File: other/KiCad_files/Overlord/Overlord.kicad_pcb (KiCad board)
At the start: 2 copper layers, 155.1 x 86.1 mm, 108 parts, among them J1 RJ45x2, J2 Screw_Terminal_01x09, J3 Conn_01x12_Female, J4 Screw_Terminal_01x09, J5 Screw_Terminal_01x09, J6 Screw_Terminal_01x09, J7 USB_B, J8 USB_cable, Q1 2N7002E, Q2 2N7002E, Q3 2N7002E, Q4 2N7002E, U1 74HC4052D,653, U2 74HC4052D,653, U3 74HC4052D,653, U4 74HC4052D,653, U5 LM2575D2T-5G, U6 SN65HVD230, U7 MAX485ESA+T, U8 AP63203WU-7, U9 MAX485ESA+T

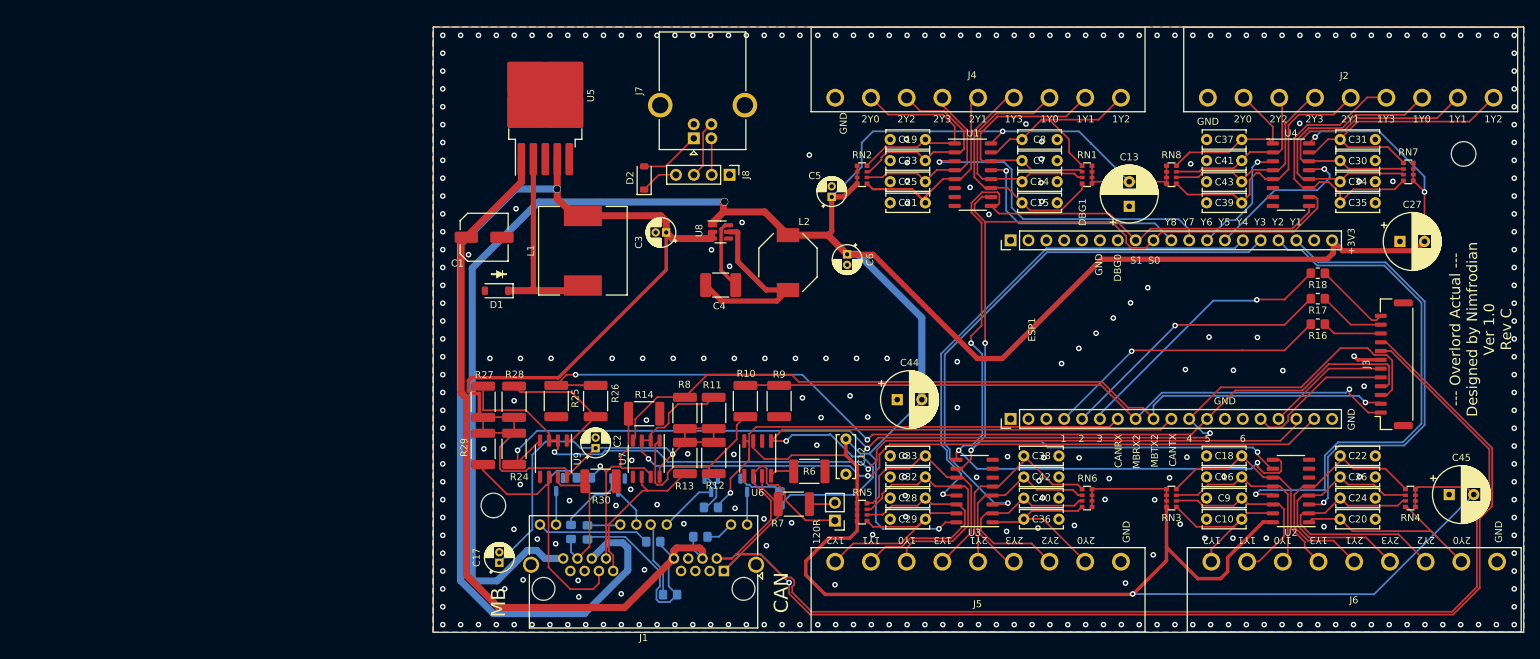
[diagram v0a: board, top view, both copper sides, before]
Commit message: sent to production
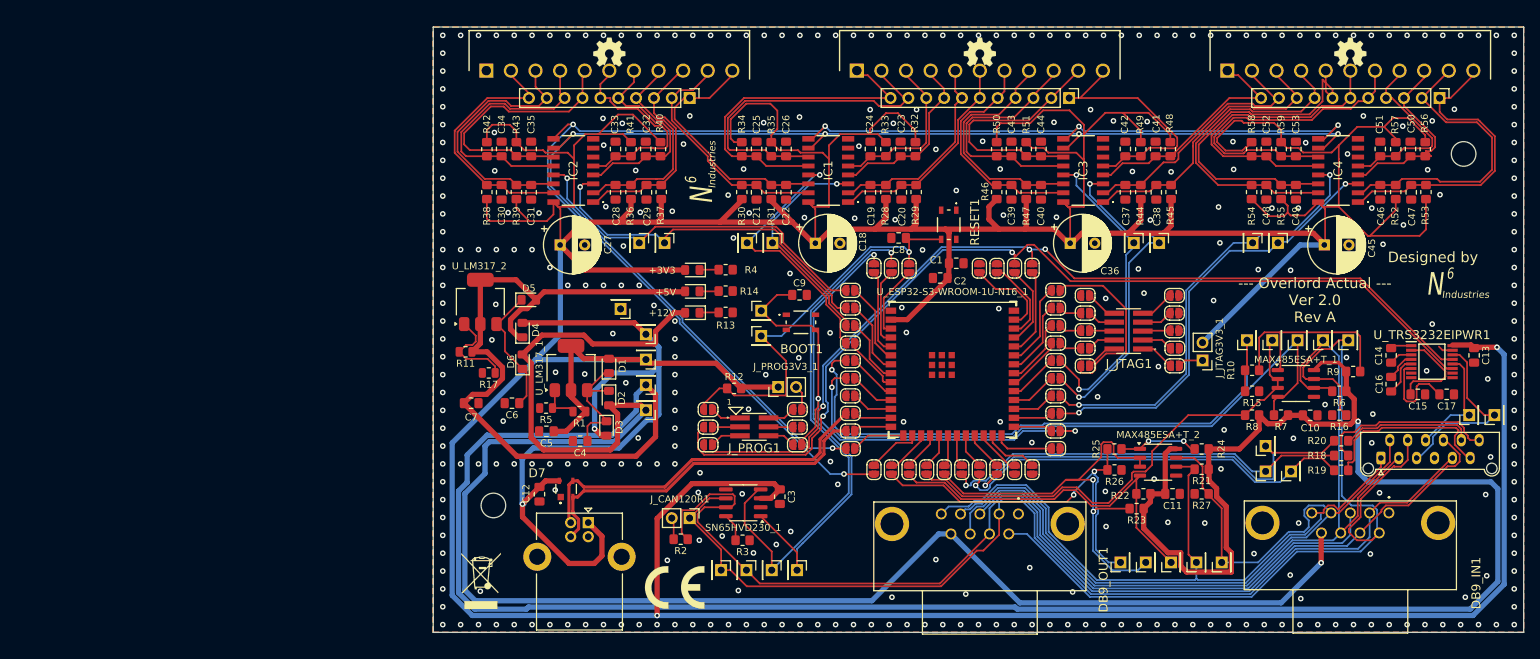
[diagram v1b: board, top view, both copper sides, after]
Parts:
- removed 120R_enable1: Conn_01x02_Male, Connector_PinHeader_2.54mm:PinHeader_1x02_P2.54mm_Vertical
- removed ESP1: ESP-DevKitC-V4, Overlord:ESP32-DevKitC-V4
- removed J8: USB_cable, Connector_PinHeader_2.54mm:PinHeader_1x04_P2.54mm_Vertical
- removed L1: 7447709331, Inductor_SMD:L_12x12mm_H8mm
- removed L2: 4.7uH, Inductor_SMD:L_Bourns-SRU8028_8.0x8.0mm
- removed Q1, Q2, Q3, Q4: 2N7002E, Package_TO_SOT_SMD:SOT-23
- removed RN1, RN2, RN3, RN4, RN5, RN6, RN7, RN8: Res_network 4.7kOhm, Resistor_SMD:R_Array_Convex_4x0612
- removed U1, U2, U3, U4: 74HC4052D,653, Package_SO:SO-16_3.9x9.9mm_P1.27mm
- removed U5: LM2575D2T-5G, Package_TO_SOT_SMD:TO-263-5_TabPin3
- removed U6: SN65HVD230, Package_SO:SOIC-8_3.9x4.9mm_P1.27mm
- removed U7, U9: MAX485ESA+T, Package_SO:SO-8_3.9x4.9mm_P1.27mm
- removed U8: AP63203WU-7, Package_TO_SOT_SMD:TSOT-23-6
- added 12VLED1: LED, LED_SMD:LED_0805_2012Metric_Pad1.15x1.40mm_HandSolder, F.Cu at (62.2, 66.0)
- added 3V3LED1: LED, LED_SMD:LED_0805_2012Metric_Pad1.15x1.40mm_HandSolder, F.Cu at (62.2, 60.0)
- added 5VLED1: LED, LED_SMD:LED_0805_2012Metric_Pad1.15x1.40mm_HandSolder, F.Cu at (62.2, 63.0)
- added BOOT1: PTS810SJK250SMTR LFS, OverlordCommon:PTS810SJK250SMTRLFS, F.Cu at (77.7, 67.4)
- added C11: 10uF, Capacitor_SMD:C_0805_2012Metric_Pad1.18x1.45mm_HandSolder, F.Cu at (130.6, 91.8)
- added C46: 0.1uF, Capacitor_SMD:C_0805_2012Metric_Pad1.18x1.45mm_HandSolder, F.Cu at (160.1, 48.9)
- added C47: 0.1uF, Capacitor_SMD:C_0805_2012Metric_Pad1.18x1.45mm_HandSolder, F.Cu at (164.5, 48.9)
- added C48: 0.1uF, Capacitor_SMD:C_0805_2012Metric_Pad1.18x1.45mm_HandSolder, F.Cu at (143.9, 48.9)
- added C49: 0.1uF, Capacitor_SMD:C_0805_2012Metric_Pad1.18x1.45mm_HandSolder, F.Cu at (148.1, 48.9)
- added C50: 0.1uF, Capacitor_SMD:C_0805_2012Metric_Pad1.18x1.45mm_HandSolder, F.Cu at (164.4, 42.7)
- added C51: 0.1uF, Capacitor_SMD:C_0805_2012Metric_Pad1.18x1.45mm_HandSolder, F.Cu at (160.1, 42.7)
- added C52: 0.1uF, Capacitor_SMD:C_0805_2012Metric_Pad1.18x1.45mm_HandSolder, F.Cu at (143.9, 42.7)
- added C53: 0.1uF, Capacitor_SMD:C_0805_2012Metric_Pad1.18x1.45mm_HandSolder, F.Cu at (148.1, 42.7)
- added D3: 1N4148, Diode_SMD:D_0805_2012Metric_Pad1.15x1.40mm_HandSolder, F.Cu at (50.0, 82.5)
- added D4: 1N4148, Diode_SMD:D_0805_2012Metric_Pad1.15x1.40mm_HandSolder, F.Cu at (38.1, 68.5)
- added D5: 1N4148, Diode_SMD:D_0805_2012Metric_Pad1.15x1.40mm_HandSolder, F.Cu at (39.0, 64.2)
- added D6: 1N4148, Diode_SMD:D_0805_2012Metric_Pad1.15x1.40mm_HandSolder, F.Cu at (38.1, 73.0)
- added D7: TPD2E001DZDR, OverlordCommon:TPD2E001DZDR, F.Cu at (44.3, 91.1)
- added DB9_IN1: 5788792-2, OverlordCommon:5788792, F.Cu at (155.8, 101.9)
- added DB9_OUT1: 5747844-4, OverlordCommon:57478444, F.Cu at (103.2, 102.0)
- added Dbg1: Connector_Conn_01x01_Male, Connector_PinHeader_2.54mm:PinHeader_1x01_P2.54mm_Vertical, F.Cu at (125.1, 56.1)
- added Dbg10: Connector_Conn_01x01_Male, Connector_PinHeader_2.54mm:PinHeader_1x01_P2.54mm_Vertical, F.Cu at (155.6, 70.0)
- added Dbg11: Connector_Conn_01x01_Male, Connector_PinHeader_2.54mm:PinHeader_1x01_P2.54mm_Vertical, F.Cu at (58.3, 56.1)
- added Dbg12: Connector_Conn_01x01_Male, Connector_PinHeader_2.54mm:PinHeader_1x01_P2.54mm_Vertical, F.Cu at (123.2, 101.5)
- added Dbg13: Connector_Conn_01x01_Male, Connector_PinHeader_2.54mm:PinHeader_1x01_P2.54mm_Vertical, F.Cu at (141.9, 56.1)
- added Dbg14: Connector_Conn_01x01_Male, Connector_PinHeader_2.54mm:PinHeader_1x01_P2.54mm_Vertical, F.Cu at (126.8, 101.5)
- added Dbg15: Connector_Conn_01x01_Male, Connector_PinHeader_2.54mm:PinHeader_1x01_P2.54mm_Vertical, F.Cu at (145.6, 56.1)
- added Dbg16: Connector_Conn_01x01_Male, Connector_PinHeader_2.54mm:PinHeader_1x01_P2.54mm_Vertical, F.Cu at (130.3, 101.5)
- added Dbg17: Connector_Conn_01x01_Male, Connector_PinHeader_2.54mm:PinHeader_1x01_P2.54mm_Vertical, F.Cu at (133.9, 101.5)
- added Dbg18: Connector_Conn_01x01_Male, Connector_PinHeader_2.54mm:PinHeader_1x01_P2.54mm_Vertical, F.Cu at (137.6, 101.5)
- added Dbg19: Connector_Conn_01x01_Male, Connector_PinHeader_2.54mm:PinHeader_1x01_P2.54mm_Vertical, F.Cu at (52.0, 65.5)
- added Dbg2: Connector_Conn_01x01_Male, Connector_PinHeader_2.54mm:PinHeader_1x01_P2.54mm_Vertical, F.Cu at (141.2, 70.0)
- added Dbg20: Connector_Conn_01x01_Male, Connector_PinHeader_2.54mm:PinHeader_1x01_P2.54mm_Vertical, F.Cu at (77.1, 102.7)
- added Dbg21: Connector_Conn_01x01_Male, Connector_PinHeader_2.54mm:PinHeader_1x01_P2.54mm_Vertical, F.Cu at (73.5, 102.7)
- added Dbg22: Connector_Conn_01x01_Male, Connector_PinHeader_2.54mm:PinHeader_1x01_P2.54mm_Vertical, F.Cu at (70.0, 102.7)
- added Dbg23: Connector_Conn_01x01_Male, Connector_PinHeader_2.54mm:PinHeader_1x01_P2.54mm_Vertical, F.Cu at (55.6, 69.1)
- added Dbg24: Connector_Conn_01x01_Male, Connector_PinHeader_2.54mm:PinHeader_1x01_P2.54mm_Vertical, F.Cu at (66.3, 102.7)
- added Dbg25: Connector_Conn_01x01_Male, Connector_PinHeader_2.54mm:PinHeader_1x01_P2.54mm_Vertical, F.Cu at (72.0, 69.3)
- added Dbg26: Connector_Conn_01x01_Male, Connector_PinHeader_2.54mm:PinHeader_1x01_P2.54mm_Vertical, F.Cu at (72.0, 65.8)
- added Dbg27: Connector_Conn_01x01_Male, Connector_PinHeader_2.54mm:PinHeader_1x01_P2.54mm_Vertical, F.Cu at (55.6, 72.7)
- added Dbg28: Connector_Conn_01x01_Male, Connector_PinHeader_2.54mm:PinHeader_1x01_P2.54mm_Vertical, F.Cu at (143.8, 88.6)
- added Dbg29: Connector_Conn_01x01_Male, Connector_PinHeader_2.54mm:PinHeader_1x01_P2.54mm_Vertical, F.Cu at (147.4, 88.6)
- added Dbg3: Connector_Conn_01x01_Male, Connector_PinHeader_2.54mm:PinHeader_1x01_P2.54mm_Vertical, F.Cu at (128.7, 56.1)
- added Dbg30: Connector_Conn_01x01_Male, Connector_PinHeader_2.54mm:PinHeader_1x01_P2.54mm_Vertical, F.Cu at (55.6, 76.3)
- added Dbg31: Connector_Conn_01x01_Male, Connector_PinHeader_2.54mm:PinHeader_1x01_P2.54mm_Vertical, F.Cu at (143.8, 85.0)
- added Dbg32: Connector_Conn_01x01_Male, Connector_PinHeader_2.54mm:PinHeader_1x01_P2.54mm_Vertical, F.Cu at (172.7, 80.6)
- added Dbg33: Connector_Conn_01x01_Male, Connector_PinHeader_2.54mm:PinHeader_1x01_P2.54mm_Vertical, F.Cu at (55.6, 79.9)
- added Dbg34: Connector_Conn_01x01_Male, Connector_PinHeader_2.54mm:PinHeader_1x01_P2.54mm_Vertical, F.Cu at (176.3, 80.6)
- added Dbg4: Connector_Conn_01x01_Male, Connector_PinHeader_2.54mm:PinHeader_1x01_P2.54mm_Vertical, F.Cu at (144.8, 70.0)
- added Dbg5: Connector_Conn_01x01_Male, Connector_PinHeader_2.54mm:PinHeader_1x01_P2.54mm_Vertical, F.Cu at (70.0, 56.1)
- added Dbg6: Connector_Conn_01x01_Male, Connector_PinHeader_2.54mm:PinHeader_1x01_P2.54mm_Vertical, F.Cu at (148.3, 70.0)
- added Dbg7: Connector_Conn_01x01_Male, Connector_PinHeader_2.54mm:PinHeader_1x01_P2.54mm_Vertical, F.Cu at (73.7, 56.1)
- added Dbg8: Connector_Conn_01x01_Male, Connector_PinHeader_2.54mm:PinHeader_1x01_P2.54mm_Vertical, F.Cu at (151.9, 70.0)
- added Dbg9: Connector_Conn_01x01_Male, Connector_PinHeader_2.54mm:PinHeader_1x01_P2.54mm_Vertical, F.Cu at (54.7, 56.1)
- added IC1: 74HC4052D,653, OverlordCommon:74HC4052D653, F.Cu at (81.6, 45.8)
- added IC2: 74HC4052D,653, OverlordCommon:74HC4052D653, F.Cu at (45.3, 45.8)
- added IC3: 74HC4052D,653, OverlordCommon:74HC4052D653, F.Cu at (117.8, 45.8)
- added IC4: 74HC4052D,653, OverlordCommon:74HC4052D653, F.Cu at (154.1, 45.8)
- added JP1: SolderJumper_2_Open, Jumper:SolderJumper-2_P1.3mm_Open_RoundedPad1.0x1.5mm, F.Cu at (103.1, 59.7)
- added JP10: SolderJumper_2_Open, Jumper:SolderJumper-2_P1.3mm_Open_RoundedPad1.0x1.5mm, F.Cu at (84.7, 65.4)
- added JP11: SolderJumper_2_Open, Jumper:SolderJumper-2_P1.3mm_Open_RoundedPad1.0x1.5mm, F.Cu at (113.9, 65.4)
- added JP12: SolderJumper_2_Open, Jumper:SolderJumper-2_P1.3mm_Open_RoundedPad1.0x1.5mm, F.Cu at (84.7, 67.9)
- added JP13: SolderJumper_2_Open, Jumper:SolderJumper-2_P1.3mm_Open_RoundedPad1.0x1.5mm, F.Cu at (113.9, 67.9)
- added JP14: SolderJumper_2_Open, Jumper:SolderJumper-2_P1.3mm_Open_RoundedPad1.0x1.5mm, F.Cu at (84.7, 70.4)
- added JP15: SolderJumper_2_Open, Jumper:SolderJumper-2_P1.3mm_Open_RoundedPad1.0x1.5mm, F.Cu at (113.9, 70.4)
- added JP16: SolderJumper_2_Open, Jumper:SolderJumper-2_P1.3mm_Open_RoundedPad1.0x1.5mm, F.Cu at (84.7, 72.9)
- added JP17: SolderJumper_2_Open, Jumper:SolderJumper-2_P1.3mm_Open_RoundedPad1.0x1.5mm, F.Cu at (113.9, 72.9)
- added JP18: SolderJumper_2_Open, Jumper:SolderJumper-2_P1.3mm_Open_RoundedPad1.0x1.5mm, F.Cu at (84.7, 75.4)
- added JP19: SolderJumper_2_Open, Jumper:SolderJumper-2_P1.3mm_Open_RoundedPad1.0x1.5mm, F.Cu at (113.9, 75.4)
- added JP2: SolderJumper_2_Open, Jumper:SolderJumper-2_P1.3mm_Open_RoundedPad1.0x1.5mm, F.Cu at (93.1, 59.7)
- added JP20: SolderJumper_2_Open, Jumper:SolderJumper-2_P1.3mm_Open_RoundedPad1.0x1.5mm, F.Cu at (84.7, 77.9)
- added JP21: SolderJumper_2_Open, Jumper:SolderJumper-2_P1.3mm_Open_RoundedPad1.0x1.5mm, F.Cu at (113.9, 77.9)
- added JP22: SolderJumper_2_Open, Jumper:SolderJumper-2_P1.3mm_Open_RoundedPad1.0x1.5mm, F.Cu at (84.7, 80.4)
- added JP23: SolderJumper_2_Open, Jumper:SolderJumper-2_P1.3mm_Open_RoundedPad1.0x1.5mm, F.Cu at (113.9, 80.4)
- added JP24: SolderJumper_2_Open, Jumper:SolderJumper-2_P1.3mm_Open_RoundedPad1.0x1.5mm, F.Cu at (84.7, 82.9)
- added JP25: SolderJumper_2_Open, Jumper:SolderJumper-2_P1.3mm_Open_RoundedPad1.0x1.5mm, F.Cu at (113.9, 82.9)
- added JP26: SolderJumper_2_Open, Jumper:SolderJumper-2_P1.3mm_Open_RoundedPad1.0x1.5mm, F.Cu at (84.7, 85.4)
- added JP27: SolderJumper_2_Open, Jumper:SolderJumper-2_P1.3mm_Open_RoundedPad1.0x1.5mm, F.Cu at (88.1, 88.4)
- added JP28: SolderJumper_2_Open, Jumper:SolderJumper-2_P1.3mm_Open_RoundedPad1.0x1.5mm, F.Cu at (90.6, 88.4)
- added JP29: SolderJumper_2_Open, Jumper:SolderJumper-2_P1.3mm_Open_RoundedPad1.0x1.5mm, F.Cu at (93.1, 88.4)
- added JP3: SolderJumper_2_Open, Jumper:SolderJumper-2_P1.3mm_Open_RoundedPad1.0x1.5mm, F.Cu at (105.6, 59.7)
- added JP30: SolderJumper_2_Open, Jumper:SolderJumper-2_P1.3mm_Open_RoundedPad1.0x1.5mm, F.Cu at (95.6, 88.4)
- added JP31: SolderJumper_2_Open, Jumper:SolderJumper-2_P1.3mm_Open_RoundedPad1.0x1.5mm, F.Cu at (98.1, 88.4)
- added JP32: SolderJumper_2_Open, Jumper:SolderJumper-2_P1.3mm_Open_RoundedPad1.0x1.5mm, F.Cu at (100.6, 88.4)
- added JP33: SolderJumper_2_Open, Jumper:SolderJumper-2_P1.3mm_Open_RoundedPad1.0x1.5mm, F.Cu at (103.1, 88.4)
- added JP34: SolderJumper_2_Open, Jumper:SolderJumper-2_P1.3mm_Open_RoundedPad1.0x1.5mm, F.Cu at (105.6, 88.4)
- added JP35: SolderJumper_2_Open, Jumper:SolderJumper-2_P1.3mm_Open_RoundedPad1.0x1.5mm, F.Cu at (108.1, 88.4)
- added JP36: SolderJumper_2_Open, Jumper:SolderJumper-2_P1.3mm_Open_RoundedPad1.0x1.5mm, F.Cu at (110.6, 88.4)
- added JP37: SolderJumper_2_Open, Jumper:SolderJumper-2_P1.3mm_Open_RoundedPad1.0x1.5mm, F.Cu at (113.9, 85.4)
- added JP38: SolderJumper_2_Open, Jumper:SolderJumper-2_P1.3mm_Open_RoundedPad1.0x1.5mm, F.Cu at (130.9, 73.6)
- added JP39: SolderJumper_2_Open, Jumper:SolderJumper-2_P1.3mm_Open_RoundedPad1.0x1.5mm, F.Cu at (118.1, 73.6)
- added JP4: SolderJumper_2_Open, Jumper:SolderJumper-2_P1.3mm_Open_RoundedPad1.0x1.5mm, F.Cu at (90.6, 59.7)
- added JP40: SolderJumper_2_Open, Jumper:SolderJumper-2_P1.3mm_Open_RoundedPad1.0x1.5mm, F.Cu at (130.9, 71.1)
- added JP41: SolderJumper_2_Open, Jumper:SolderJumper-2_P1.3mm_Open_RoundedPad1.0x1.5mm, F.Cu at (118.1, 71.1)
- added JP42: SolderJumper_2_Open, Jumper:SolderJumper-2_P1.3mm_Open_RoundedPad1.0x1.5mm, F.Cu at (130.8, 68.6)
- added JP43: SolderJumper_2_Open, Jumper:SolderJumper-2_P1.3mm_Open_RoundedPad1.0x1.5mm, F.Cu at (118.1, 68.6)
- added JP44: SolderJumper_2_Open, Jumper:SolderJumper-2_P1.3mm_Open_RoundedPad1.0x1.5mm, F.Cu at (130.8, 66.1)
- added JP45: SolderJumper_2_Open, Jumper:SolderJumper-2_P1.3mm_Open_RoundedPad1.0x1.5mm, F.Cu at (118.1, 66.1)
- added JP46: SolderJumper_2_Open, Jumper:SolderJumper-2_P1.3mm_Open_RoundedPad1.0x1.5mm, F.Cu at (130.8, 63.6)
- added JP47: SolderJumper_2_Open, Jumper:SolderJumper-2_P1.3mm_Open_RoundedPad1.0x1.5mm, F.Cu at (118.1, 63.6)
- added JP48: SolderJumper_2_Open, Jumper:SolderJumper-2_P1.3mm_Open_RoundedPad1.0x1.5mm, F.Cu at (64.5, 79.8)
- added JP49: SolderJumper_2_Open, Jumper:SolderJumper-2_P1.3mm_Open_RoundedPad1.0x1.5mm, F.Cu at (77.2, 79.8)
- added JP5: SolderJumper_2_Open, Jumper:SolderJumper-2_P1.3mm_Open_RoundedPad1.0x1.5mm, F.Cu at (108.1, 59.7)
- added JP50: SolderJumper_2_Open, Jumper:SolderJumper-2_P1.3mm_Open_RoundedPad1.0x1.5mm, F.Cu at (64.5, 82.3)
- added JP51: SolderJumper_2_Open, Jumper:SolderJumper-2_P1.3mm_Open_RoundedPad1.0x1.5mm, F.Cu at (77.2, 82.3)
- added JP52: SolderJumper_2_Open, Jumper:SolderJumper-2_P1.3mm_Open_RoundedPad1.0x1.5mm, F.Cu at (64.5, 84.8)
- added JP53: SolderJumper_2_Open, Jumper:SolderJumper-2_P1.3mm_Open_RoundedPad1.0x1.5mm, F.Cu at (77.2, 84.8)
- added JP6: SolderJumper_2_Open, Jumper:SolderJumper-2_P1.3mm_Open_RoundedPad1.0x1.5mm, F.Cu at (88.1, 59.7)
- added JP7: SolderJumper_2_Open, Jumper:SolderJumper-2_P1.3mm_Open_RoundedPad1.0x1.5mm, F.Cu at (110.6, 59.7)
- added JP8: SolderJumper_2_Open, Jumper:SolderJumper-2_P1.3mm_Open_RoundedPad1.0x1.5mm, F.Cu at (84.7, 62.9)
- added JP9: SolderJumper_2_Open, Jumper:SolderJumper-2_P1.3mm_Open_RoundedPad1.0x1.5mm, F.Cu at (113.9, 62.9)
- added J_CAN120R1: Conn_01x02_Male, Connector_PinHeader_2.54mm:PinHeader_1x02_P2.54mm_Vertical, F.Cu at (61.9, 95.2)
- added J_JTAG1: FTSH-105-01-S-DV-K, OverlordCommon:FTSH-105-XX-YYY-DV-K, F.Cu at (124.3, 68.7)
- added J_JTAG3V3_1: Conn_01x02_Pin, Connector_PinHeader_2.54mm:PinHeader_1x02_P2.54mm_Vertical, F.Cu at (134.8, 72.8)
- added J_PROG1: FTSH-103-01-S-DV-TR, OverlordCommon:FTSH-103-XX-YYY-DV-TR, F.Cu at (71.1, 82.3)
- added J_PROG3V3_1: Conn_01x02_Pin, Connector_PinHeader_2.54mm:PinHeader_1x02_P2.54mm_Vertical, F.Cu at (74.5, 76.6)
- added J_USB1: USB_B, OverlordCommon:USB, F.Cu at (46.2, 102.9)
- added MAX485ESA+T_1: MAX485ESA+T, Package_SO:SO-8_3.9x4.9mm_P1.27mm, F.Cu at (148.1, 76.1)
- added MAX485ESA+T_2: MAX485ESA+T, Package_SO:SO-8_3.9x4.9mm_P1.27mm, F.Cu at (128.5, 87.3)
- added R19: 220, Resistor_SMD:R_0805_2012Metric_Pad1.20x1.40mm_HandSolder, F.Cu at (154.6, 88.5)
- added R20: 220, Resistor_SMD:R_0805_2012Metric_Pad1.20x1.40mm_HandSolder, F.Cu at (154.6, 84.2)
- added R21: 20K, Resistor_SMD:R_0805_2012Metric_Pad1.20x1.40mm_HandSolder, F.Cu at (134.7, 88.3)
- added R22: 10K, Resistor_SMD:R_0805_2012Metric_Pad1.20x1.40mm_HandSolder, F.Cu at (126.4, 91.8)
- added R23: 10K, Resistor_SMD:R_0805_2012Metric_Pad1.20x1.40mm_HandSolder, F.Cu at (125.5, 93.9)
- added R32: 4.7k, Resistor_SMD:R_0805_2012Metric_Pad1.20x1.40mm_HandSolder, F.Cu at (94.0, 42.8)
- added R34: 4.7k, Resistor_SMD:R_0805_2012Metric_Pad1.20x1.40mm_HandSolder, F.Cu at (69.3, 42.8)
- added R35: 4.7k, Resistor_SMD:R_0805_2012Metric_Pad1.20x1.40mm_HandSolder, F.Cu at (73.5, 42.8)
- added R36: 4.7k, Resistor_SMD:R_0805_2012Metric_Pad1.20x1.40mm_HandSolder, F.Cu at (53.5, 48.9)
- added R37: 4.7k, Resistor_SMD:R_0805_2012Metric_Pad1.20x1.40mm_HandSolder, F.Cu at (57.8, 48.9)
- added R38: 4.7k, Resistor_SMD:R_0805_2012Metric_Pad1.20x1.40mm_HandSolder, F.Cu at (33.0, 48.9)
- added R39: 4.7k, Resistor_SMD:R_0805_2012Metric_Pad1.20x1.40mm_HandSolder, F.Cu at (37.2, 48.9)
- added R40: 4.7k, Resistor_SMD:R_0805_2012Metric_Pad1.20x1.40mm_HandSolder, F.Cu at (57.7, 42.8)
- added R41: 4.7k, Resistor_SMD:R_0805_2012Metric_Pad1.20x1.40mm_HandSolder, F.Cu at (53.5, 42.8)
- added R42: 4.7k, Resistor_SMD:R_0805_2012Metric_Pad1.20x1.40mm_HandSolder, F.Cu at (33.0, 42.8)
- added R43: 4.7k, Resistor_SMD:R_0805_2012Metric_Pad1.20x1.40mm_HandSolder, F.Cu at (37.2, 42.8)
- added R44: 4.7k, Resistor_SMD:R_0805_2012Metric_Pad1.20x1.40mm_HandSolder, F.Cu at (126.0, 48.9)
- added R45: 4.7k, Resistor_SMD:R_0805_2012Metric_Pad1.20x1.40mm_HandSolder, F.Cu at (130.3, 48.9)
- added R46: 4.7k, Resistor_SMD:R_0805_2012Metric_Pad1.20x1.40mm_HandSolder, F.Cu at (105.5, 48.9)
- added R47: 4.7k, Resistor_SMD:R_0805_2012Metric_Pad1.20x1.40mm_HandSolder, F.Cu at (109.7, 48.9)
- added R48: 4.7k, Resistor_SMD:R_0805_2012Metric_Pad1.20x1.40mm_HandSolder, F.Cu at (130.2, 42.8)
- added R49: 4.7k, Resistor_SMD:R_0805_2012Metric_Pad1.20x1.40mm_HandSolder, F.Cu at (126.0, 42.8)
- added R50: 4.7k, Resistor_SMD:R_0805_2012Metric_Pad1.20x1.40mm_HandSolder, F.Cu at (105.5, 42.8)
- added R51: 4.7k, Resistor_SMD:R_0805_2012Metric_Pad1.20x1.40mm_HandSolder, F.Cu at (109.7, 42.8)
- added R52: 4.7k, Resistor_SMD:R_0805_2012Metric_Pad1.20x1.40mm_HandSolder, F.Cu at (162.3, 48.9)
- added R53: 4.7k, Resistor_SMD:R_0805_2012Metric_Pad1.20x1.40mm_HandSolder, F.Cu at (166.6, 48.9)
- added R54: 4.7k, Resistor_SMD:R_0805_2012Metric_Pad1.20x1.40mm_HandSolder, F.Cu at (141.8, 48.9)
- added R55: 4.7k, Resistor_SMD:R_0805_2012Metric_Pad1.20x1.40mm_HandSolder, F.Cu at (146.0, 48.9)
- added R56: 4.7k, Resistor_SMD:R_0805_2012Metric_Pad1.20x1.40mm_HandSolder, F.Cu at (166.5, 42.8)
- added R57: 4.7k, Resistor_SMD:R_0805_2012Metric_Pad1.20x1.40mm_HandSolder, F.Cu at (162.3, 42.8)
- added R58: 4.7k, Resistor_SMD:R_0805_2012Metric_Pad1.20x1.40mm_HandSolder, F.Cu at (141.8, 42.8)
- added R59: 4.7k, Resistor_SMD:R_0805_2012Metric_Pad1.20x1.40mm_HandSolder, F.Cu at (146.0, 42.8)
- added RESET1: PTS810SJK250SMTR LFS, OverlordCommon:PTS810SJK250SMTRLFS, F.Cu at (98.7, 53.5)
- added SN65HVD230_1: SN65HVD230, Package_SO:SOIC-8_3.9x4.9mm_P1.27mm, F.Cu at (69.5, 93.1)
- added SYM1: Terminal plug, OverlordCommon:39500-0011, F.Cu at (50.5, 29.1)
- added SYM2: Terminal plug, OverlordCommon:39500-0011, F.Cu at (155.9, 29.1)
- added SYM3: Terminal plug, OverlordCommon:39500-0011, F.Cu at (103.2, 29.1)
- added SYM4: N6_logo_medium, OverlordCommon:Symbol_N6Industries_medium, F.Cu at (64.0, 45.9)
- added SYM5: N6_logo_medium, OverlordCommon:Symbol_N6Industries_medium, F.Cu at (171.3, 62.4)
- added SYM6: WEEE, Symbol:WEEE-Logo_5.6x8mm_SilkScreen, F.Cu at (32.2, 104.2)
- added SYM7: CE, Symbol:CE-Logo_8.5x6mm_SilkScreen, F.Cu at (59.8, 105.1)
- added U_ESP32-S3-WROOM-1U-N16_1: ESP32S3-Wroom, PCM_Espressif:ESP32-S3-WROOM-1U, F.Cu at (99.3, 74.0)
- added U_LM317_1: LM317_SOT-223, Package_TO_SOT_SMD:SOT-223-3_TabPin2, F.Cu at (45.0, 73.9)
- added U_LM317_2: LM317_SOT-223, Package_TO_SOT_SMD:SOT-223-3_TabPin2, F.Cu at (32.1, 64.5)
- added U_TRS3232EIPWR1: TRS3232EIPWR, OverlordCommon:SOP65P640X120-16N, F.Cu at (167.4, 73.0)
- C1: value 100uF -> 0.1uF; footprint Capacitor_SMD:C_Elec_6.3x7.7 -> Capacitor_SMD:C_0805_2012Metric_Pad1.18x1.45mm_HandSolder
- C10: value 100nF -> 10uF; footprint Capacitor_THT:C_Disc_D6.0mm_W2.5mm_P5.00mm -> Capacitor_SMD:C_0805_2012Metric_Pad1.18x1.45mm_HandSolder
- C12, C14, C15, C16, C19, C20, C21, C22, C23, C24, C25, C26, C28, C29, C30, C31, C32, C33, C34, C35, C37, C38, C39, C40, C41, C42, C43, C8, C9: value 100nF -> 0.1uF; footprint Capacitor_THT:C_Disc_D6.0mm_W2.5mm_P5.00mm -> Capacitor_SMD:C_0805_2012Metric_Pad1.18x1.45mm_HandSolder
- C13, C44: value 220uF -> 0.1uF; footprint Capacitor_THT:CP_Radial_D8.0mm_P3.50mm -> Capacitor_SMD:C_0805_2012Metric_Pad1.18x1.45mm_HandSolder
- C17, C3: value 10uF -> 0.1uF; footprint Capacitor_THT:CP_Radial_D4.0mm_P1.50mm -> Capacitor_SMD:C_0805_2012Metric_Pad1.18x1.45mm_HandSolder
- C18, C36: value 100nF -> 220uF; footprint Capacitor_THT:C_Disc_D6.0mm_W2.5mm_P5.00mm -> Capacitor_THT:CP_Radial_D8.0mm_P3.50mm
- C2: footprint Capacitor_THT:CP_Radial_D4.0mm_P1.50mm -> Capacitor_SMD:C_0805_2012Metric_Pad1.18x1.45mm_HandSolder
- C4: value 100nF -> 1uF; footprint Capacitor_SMD:C_1812_4532Metric_Pad1.57x3.40mm_HandSolder -> Capacitor_SMD:C_0805_2012Metric_Pad1.18x1.45mm_HandSolder
- C5, C6: value 22uF -> 1uF; footprint Capacitor_THT:CP_Radial_D4.0mm_P1.50mm -> Capacitor_SMD:C_0805_2012Metric_Pad1.18x1.45mm_HandSolder
- C7: value 100nF -> 1uF; footprint Capacitor_THT:C_Disc_D6.0mm_W2.5mm_P5.00mm -> Capacitor_SMD:C_0805_2012Metric_Pad1.18x1.45mm_HandSolder
- D1: value 1N5819 -> 1N4148; footprint Diode_SMD:D_SOD-123 -> Diode_SMD:D_0805_2012Metric_Pad1.15x1.40mm_HandSolder
- D2: value D -> 1N4148; footprint Diode_SMD:D_SOD-123 -> Diode_SMD:D_0805_2012Metric_Pad1.15x1.40mm_HandSolder
- J1: value RJ45x2 -> 39502-1011; footprint Connector_RJ:RJ45_Amphenol_RJHSE538X-02 -> OverlordCommon:SHDRRA11W80P0X350_1X11_3990X690X920P
- J2: value Screw_Terminal_01x09 -> 39502-1011; footprint TerminalBlockCustom:TerminalBlock_9_5.08mm_inverted -> OverlordCommon:SHDRRA11W80P0X350_1X11_3990X690X920P
- J3: value Conn_01x12_Female -> 39502-1011; footprint Connector_Molex:Molex_CLIK-Mate_502386-1270_1x12-1MP_P1.25mm_Horizontal -> OverlordCommon:SHDRRA11W80P0X350_1X11_3990X690X920P
- J4: value Screw_Terminal_01x09 -> Conn_01x12_Pin; footprint TerminalBlockCustom:TerminalBlock_9_5.08mm -> Connector_Molex:Molex_Picoflex_90325-0012_2x06_P1.27mm_Vertical
- J5: value Screw_Terminal_01x09 -> Conn_01x10_Pin; footprint TerminalBlockCustom:TerminalBlock_9_5.08mm_inverted -> Connector_PinHeader_2.54mm:PinHeader_1x10_P2.54mm_Vertical
- J6: value Screw_Terminal_01x09 -> Conn_01x11_Pin; footprint TerminalBlockCustom:TerminalBlock_9_5.08mm_inverted -> Connector_PinHeader_2.54mm:PinHeader_1x11_P2.54mm_Vertical
- J7: value USB_B -> Conn_01x11_Pin; footprint Connector_USB:USB_B_OST_USB-B1HSxx_Horizontal -> Connector_PinHeader_2.54mm:PinHeader_1x11_P2.54mm_Vertical
- R1: value 5K -> 240; footprint Resistor_SMD:R_0805_2012Metric_Pad1.20x1.40mm_HandSolder -> Resistor_SMD:R_0805_2012Metric; moved to F.Cu
- R10, R24, R6, R8: footprint Resistor_SMD:R_1812_4532Metric_Pad1.30x3.40mm_HandSolder -> Resistor_SMD:R_0805_2012Metric_Pad1.20x1.40mm_HandSolder
- R11: value 10K -> 240; footprint Resistor_SMD:R_1812_4532Metric_Pad1.30x3.40mm_HandSolder -> Resistor_SMD:R_0805_2012Metric
- R12: value 10K -> 10k; footprint Resistor_SMD:R_1812_4532Metric_Pad1.30x3.40mm_HandSolder -> Resistor_SMD:R_0805_2012Metric_Pad1.20x1.40mm_HandSolder
- R13: value 20K -> 499; footprint Resistor_SMD:R_1812_4532Metric_Pad1.30x3.40mm_HandSolder -> Resistor_SMD:R_0805_2012Metric_Pad1.20x1.40mm_HandSolder
- R14: value 20K -> 147; footprint Resistor_SMD:R_1812_4532Metric_Pad1.30x3.40mm_HandSolder -> Resistor_SMD:R_0805_2012Metric_Pad1.20x1.40mm_HandSolder
- R15: value 10K -> 6K8; moved to F.Cu
- R16: value 220 -> 20K
- R17: value 220 -> 680; footprint Resistor_SMD:R_0805_2012Metric_Pad1.20x1.40mm_HandSolder -> Resistor_SMD:R_0805_2012Metric
- R2: value 5K -> 120; moved to F.Cu
- R25: value 6K8 -> 3K3; footprint Resistor_SMD:R_1812_4532Metric_Pad1.30x3.40mm_HandSolder -> Resistor_SMD:R_0805_2012Metric_Pad1.20x1.40mm_HandSolder
- R26: value 3K3 -> 6K8; footprint Resistor_SMD:R_1812_4532Metric_Pad1.30x3.40mm_HandSolder -> Resistor_SMD:R_0805_2012Metric_Pad1.20x1.40mm_HandSolder
- R27: value 10K -> 20K; footprint Resistor_SMD:R_1812_4532Metric_Pad1.30x3.40mm_HandSolder -> Resistor_SMD:R_0805_2012Metric_Pad1.20x1.40mm_HandSolder
- R28: value 10K -> 4.7k; footprint Resistor_SMD:R_1812_4532Metric_Pad1.30x3.40mm_HandSolder -> Resistor_SMD:R_0805_2012Metric_Pad1.20x1.40mm_HandSolder
- R29, R30: value 20K -> 4.7k; footprint Resistor_SMD:R_1812_4532Metric_Pad1.30x3.40mm_HandSolder -> Resistor_SMD:R_0805_2012Metric_Pad1.20x1.40mm_HandSolder
- R3: value 10K -> 0R; moved to F.Cu
- R31, R33: value 5K -> 4.7k; moved to F.Cu
- R4: value 10K -> 60; moved to F.Cu
- R5: value 10K -> 390; footprint Resistor_SMD:R_0805_2012Metric_Pad1.20x1.40mm_HandSolder -> Resistor_SMD:R_0805_2012Metric; moved to F.Cu
- R7: value 120 -> 10K; footprint Resistor_SMD:R_1812_4532Metric_Pad1.30x3.40mm_HandSolder -> Resistor_SMD:R_0805_2012Metric_Pad1.20x1.40mm_HandSolder
- R9: value 6K8 -> 10K; footprint Resistor_SMD:R_1812_4532Metric_Pad1.30x3.40mm_HandSolder -> Resistor_SMD:R_0805_2012Metric_Pad1.20x1.40mm_HandSolder
- moved C17 136.9 mm to (169.6, 77.7), turned to 180 degrees
- moved C34 124.4 mm to (35.1, 42.7), turned to 90 degrees
- moved C30 124.4 mm to (35.1, 48.9), turned to 90 degrees
- moved C27 119.5 mm to (43.5, 56.4)
- moved R17 118.4 mm to (33.3, 74.6)
- moved C35 115.3 mm to (39.3, 42.7), turned to 90 degrees
- moved C31 115.3 mm to (39.3, 48.9), turned to 90 degrees
- moved J7 106.2 mm to (168.6, 35.5), turned to -90 degrees
- moved R27 103.0 mm to (134.7, 91.8), turned to 180 degrees
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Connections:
- C1 pad 1: +12V -> +3.3V
- C10 pad 1: 2_1Y2 -> +5V
- C12 pad 1: GND -> USB+5V
- C12 pad 2: +3.3V -> GND
- C13 pad 1: GND -> +3.3V
- C13 pad 2: +3.3V -> GND
- C14 pad 1: GND -> Net-(U_TRS3232EIPWR1-C1+)
- C14 pad 2: 1_1Y0 -> Net-(U_TRS3232EIPWR1-C1-)
- C15 pad 1: 1_1Y3 -> GND
- C15 pad 2: GND -> Net-(U_TRS3232EIPWR1-V+)
- C16 pad 1: GND -> Net-(U_TRS3232EIPWR1-C2-)
- C16 pad 2: 2_1Y0 -> Net-(U_TRS3232EIPWR1-C2+)
- C17 pad 1: +5V -> GND
- C17 pad 2: GND -> Net-(U_TRS3232EIPWR1-V-)
- C18 pad 1: 2_1Y3 -> +3.3V
- C19 pad 2: 1_2Y0 -> 3_1Y2
- C2 pad 1: +5V -> GND
- C2 pad 2: GND -> +3.3V
- C20 pad 2: 2_2Y0 -> 3_1Y0
- C21 pad 2: 1_2Y1 -> 3_2Y2
- C22 pad 2: 2_2Y1 -> 3_2Y1
- C23 pad 1: GND -> 3_1Y3
- C23 pad 2: 1_2Y2 -> GND
- C24 pad 1: GND -> 3_1Y1
- C24 pad 2: 2_2Y2 -> GND
- C25 pad 1: GND -> 3_2Y0
- C25 pad 2: 1_2Y3 -> GND
- C26 pad 1: GND -> 3_2Y3
- C26 pad 2: 2_2Y3 -> GND
- C27 pad 1: GND -> +3.3V
- C27 pad 2: +3.3V -> GND
- C28 pad 2: 3_1Y1 -> 4_1Y2
- C29 pad 1: 3_1Y2 -> GND
- C29 pad 2: GND -> 4_1Y0
- C3 pad 1: +5V -> +3.3V
- C30 pad 2: 4_1Y1 -> 4_2Y2
- C31 pad 1: 4_1Y2 -> GND
- C31 pad 2: GND -> 4_2Y1
- C32 pad 1: GND -> 4_1Y3
- C32 pad 2: 3_1Y0 -> GND
- C33 pad 1: 3_1Y3 -> 4_1Y1
- C34 pad 1: GND -> 4_2Y0
- C34 pad 2: 4_1Y0 -> GND
- C35 pad 1: 4_1Y3 -> 4_2Y3
- C36 pad 1: GND -> +3.3V
- C36 pad 2: 3_2Y0 -> GND
- C37 pad 2: 4_2Y0 -> 2_1Y2
- C38 pad 2: 3_2Y1 -> 2_1Y0
- C39 pad 2: 4_2Y1 -> 2_2Y2
- C4 pad 1: Net-(U8-SW) -> Net-(D1-K)
- C4 pad 2: Net-(U8-BST) -> GND
- C40 pad 2: 3_2Y2 -> 2_2Y1
- C41 pad 1: GND -> 2_1Y3
- C41 pad 2: 4_2Y2 -> GND
- C42 pad 1: GND -> 2_1Y1
- C42 pad 2: 3_2Y3 -> GND
- C43 pad 1: GND -> 2_2Y0
- C43 pad 2: 4_2Y3 -> GND
- C44 pad 1: GND -> 2_2Y3
- C44 pad 2: +3.3V -> GND
- C45 pad 1: GND -> +3.3V
- C45 pad 2: +3.3V -> GND
- C6 pad 1: +3.3V -> Net-(D5-K)
- C7 pad 1: GND -> +5V
- C7 pad 2: 1_1Y1 -> GND
- C8 pad 1: 1_1Y2 -> ESP_EN
- C9 pad 1: GND -> ESP_IO0
- C9 pad 2: 2_1Y1 -> GND
- D1 pad 2: GND -> +3.3V
- D2 pad 1: Net-(D2-K) -> Net-(D1-K)
- D2 pad 2: Net-(D2-A) -> +12V
- J1 pad 1: CAN_H -> GND
- J1 pad 10: Net-(J1-Pad10) -> 3_2Y2
- J1 pad 11: Net-(Q3-D) -> 3_2Y1
- J1 pad 2: CAN_L -> 4_2Y2
- J1 pad 3: unconnected-(J1-Pad3) -> 4_2Y1
- J1 pad 4: +12V -> 4_2Y0
- J1 pad 5: GND -> 4_2Y3
- J1 pad 6: unconnected-(J1-Pad6) -> 4_1Y1
- J1 pad 7: GND -> 4_1Y3
- J1 pad 8: +12V -> 4_1Y2
- J1 pad 9: Net-(Q1-D) -> 4_1Y0
- J2 pad 1: 4_1Y2 -> 3_2Y0
- J2 pad 2: 4_1Y1 -> 3_2Y3
- J2 pad 3: 4_1Y0 -> 3_1Y1
- J2 pad 4: 4_1Y3 -> 3_1Y3
- J2 pad 5: 4_2Y1 -> 3_1Y2
- J2 pad 6: 4_2Y3 -> 3_1Y0
- J2 pad 7: 4_2Y2 -> 2_2Y2
- J2 pad 8: 4_2Y0 -> 2_2Y1
- J2 pad 9: GND -> 2_2Y0
- J3 pad 1: MB_RX_U2 -> 2_1Y3
- J3 pad 10: Net-(J3-Pin_10) -> 1_1Y2
- J3 pad 11: Net-(J3-Pin_11) -> 1_1Y0
- J3 pad 2: MB_TX_U2 -> 2_1Y2
- J3 pad 3: MB_TX_U1 -> 2_1Y0
- J3 pad 4: MB_RX_U1 -> 1_2Y2
- J3 pad 5: UART_RX_0 -> 1_2Y1
- J3 pad 6: UART_TX_0 -> 1_2Y0
- J3 pad 7: GND -> 1_2Y3
- J3 pad 8: CAN_H -> 1_1Y1
- J3 pad 9: CAN_L -> 1_1Y3
- J4 pad 1: 1_1Y2 -> MB2_H
- J4 pad 2: 1_1Y1 -> MB2_L
- J4 pad 3: 1_1Y0 -> MB1_H
- J4 pad 4: 1_1Y3 -> MB1_L
- J4 pad 5: 1_2Y1 -> RS232_TX
- J4 pad 6: 1_2Y3 -> RS232_RX
- J4 pad 7: 1_2Y2 -> GND
- J4 pad 8: 1_2Y0 -> CAN_H
- J4 pad 9: GND -> CAN_L
- J5 pad 1: 3_1Y2 -> 3_2Y1
- J5 pad 2: 3_1Y1 -> 3_2Y2
- J5 pad 3: 3_1Y0 -> 4_1Y0
- J5 pad 4: 3_1Y3 -> 4_1Y2
- J5 pad 5: 3_2Y1 -> 4_1Y3
- J5 pad 6: 3_2Y3 -> 4_1Y1
- J5 pad 7: 3_2Y2 -> 4_2Y3
- J5 pad 8: 3_2Y0 -> 4_2Y0
- J5 pad 9: GND -> 4_2Y1
- J6 pad 1: 2_1Y2 -> 2_1Y1
- J6 pad 2: 2_1Y1 -> 2_2Y3
- J6 pad 3: 2_1Y0 -> 2_2Y0
- J6 pad 4: 2_1Y3 -> 2_2Y1
- J6 pad 5: 2_2Y1 -> 2_2Y2
- J6 pad 6: 2_2Y3 -> 3_1Y0
- J6 pad 7: 2_2Y2 -> 3_1Y2
- J6 pad 8: 2_2Y0 -> 3_1Y3
- J6 pad 9: GND -> 3_1Y1
- J7 pad 1: Net-(D2-A) -> 1_1Y0
- J7 pad 2: Net-(J7-D-) -> 1_1Y2
- J7 pad 3: Net-(J7-D+) -> 1_1Y3
- J7 pad 4: GND -> 1_1Y1
- J7 pad 5: GND -> 1_2Y3
- R1 pad 1: Net-(J1-Pad24) -> +3.3V
- R1 pad 2: +12V -> Net-(U_LM317_1-ADJ)
- R10 pad 1: MB_RX_U2 -> MB_RX_U1
- R10 pad 2: Net-(U7-RO) -> Net-(MAX485ESA+T_1-RO)
- R11 pad 2: MB_DIR_CTRL_U2 -> Net-(U_LM317_2-ADJ)
- R12 pad 1: +5V -> ESP_EN
- R12 pad 2: Net-(U7-RO) -> +3.3V
- R13 pad 1: +5V -> Net-(12VLED1-K)
- R13 pad 2: MB_A_2+ -> GND
- R14 pad 1: MB_B_2- -> Net-(5VLED1-K)
- R15 pad 1: Net-(Q4-G) -> GND
- R15 pad 2: MB_B_1- -> MB_RX_U1
- R16 pad 1: Net-(J3-Pin_10) -> MB1_L
- R16 pad 2: STATUS_LED_R -> GND
- R17 pad 1: Net-(J3-Pin_11) -> Net-(U_LM317_2-ADJ)
- R17 pad 2: STATUS_LED_G -> GND
- R18 pad 1: Net-(J3-Pin_12) -> Net-(J4-Pin_12)
- R18 pad 2: STATUS_LED_B -> STATUS_LED_R
- R2 pad 1: Net-(J1-Pad22) -> CAN_H
- R2 pad 2: +12V -> Net-(J_CAN120R1-Pin_2)
- R24 pad 2: MB_TX_U1 -> Net-(MAX485ESA+T_2-RO)
- R25 pad 1: GND -> MB_RX_U2
- R25 pad 2: MB_RX_U1 -> Net-(MAX485ESA+T_2-RO)
- R26 pad 1: MB_RX_U1 -> GND
- R26 pad 2: Net-(U9-RO) -> MB_RX_U2
- R27 pad 1: +5V -> MB2_L
- R27 pad 2: MB_DIR_CTRL_U1 -> GND
- R28 pad 1: +5V -> +3.3V
- R28 pad 2: Net-(U9-RO) -> 3_1Y2
- R29 pad 1: +5V -> +3.3V
- R29 pad 2: MB_A_1+ -> 3_1Y0
- R3 pad 1: Net-(Q1-G) -> GND
- R3 pad 2: CAN_TX -> Net-(SN65HVD230_1-Rs)
- R30 pad 1: MB_B_1- -> +3.3V
- R30 pad 2: GND -> 3_2Y2
- R31 pad 1: Net-(J1-Pad12) -> +3.3V
- R31 pad 2: +12V -> 3_2Y1
- R33 pad 1: Net-(J1-Pad10) -> +3.3V
- R33 pad 2: +12V -> 3_1Y1
- R4 pad 2: MB_B_2- -> GND
- R5 pad 1: Net-(Q3-G) -> Net-(U_LM317_1-ADJ)
- R5 pad 2: CAN_RX -> GND
- R6 pad 1: GND -> +5V
- R6 pad 2: Net-(U6-Rs) -> MB1_H
- R7 pad 1: CAN_H -> +5V
- R7 pad 2: Net-(120R_enable1-Pin_2) -> MB_TX_U1
- R8 pad 2: MB_TX_U2 -> MB_DIR_CTRL_U1
- R9 pad 1: GND -> +5V
- R9 pad 2: MB_RX_U2 -> Net-(MAX485ESA+T_1-RO)
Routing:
- net +3.3V: track 605.9 -> 884.8 mm, vias 6 -> 2
- net +5V: track 274.6 -> 435.5 mm, vias 2 -> 1
- net MB1_L: track 0.00 -> 134.1 mm
- net MB1_H: track 0.00 -> 122.5 mm
- net UART_TX_0: track 17.5 -> 139.1 mm, vias 0 -> 2
- net MB2_L: track 0.00 -> 121.2 mm
- net UART_RX_0: track 21.0 -> 134.0 mm, vias 0 -> 3
- net +12V: track 137.0 -> 248.4 mm, vias 0 -> 1
- net USB+5V: track 0.00 -> 105.7 mm, vias 0 -> 2
- net MB2_H: track 0.00 -> 102.9 mm
- net ESP_IO0: track 0.00 -> 74.9 mm, vias 0 -> 2
- net Pin3: track 0.00 -> 67.8 mm
- net MB_TX_U2: track 117.4 -> 52.2 mm, vias 1 -> 0
- net MB_DIR_CTRL_U1: track 129.7 -> 68.9 mm, vias 2 -> 0
- net ESP_EN: track 0.00 -> 59.2 mm, vias 0 -> 1
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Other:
- board text added: "+12V"
- board text added: "+5V"
- board text added: "--- Overlord Actual --- Ver 2.0 Rev A"
- board text added: "Designed by"
- board text removed: "--- Overlord Actual --- Designed by Nimfrodian Ver 1.0 Rev C"
- board text removed: "120R"
- board text removed: "1Y0"
- board text removed: "1Y1"
- board text removed: "1Y2"
- board text removed: "1Y3"
- board text removed: "2"
- board text removed: "2Y0"
- board text removed: "2Y1"
- board text removed: "2Y2"
- board text removed: "2Y3"
- board text removed: "3"
- board text removed: "4"
- board text removed: "5"
- board text removed: "6"
- board text removed: "CAN"
- board text removed: "CANRX"
- board text removed: "CANTX"
- board text removed: "DBG0"
- board text removed: "DBG1"
- board text removed: "GND"
- board text removed: "MB"
- board text removed: "MBRX2"
- board text removed: "MBTX2"
- board text removed: "S0"
- board text removed: "S1"
- board text removed: "Y1"
- board text removed: "Y2"
- board text removed: "Y3"
- board text removed: "Y4"
- board text removed: "Y5"
- board text removed: "Y6"
- board text removed: "Y7"
- board text removed: "Y8"

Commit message: sent to production with fixes
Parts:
- removed 3V3LED1: LED, LED_SMD:LED_0805_2012Metric_Pad1.15x1.40mm_HandSolder
- removed C5: 1uF, Capacitor_SMD:C_0805_2012Metric_Pad1.18x1.45mm_HandSolder
- removed D3, D6: 1N4148, Diode_SMD:D_0805_2012Metric_Pad1.15x1.40mm_HandSolder
- removed H1, H2: MountingHole, MountingHole:MountingHole_3.5mm
- removed JP39, JP40, JP41, JP42, JP43, JP44, JP45, JP46, JP47, JP48, JP50, JP51, JP52, JP53: SolderJumper_2_Open, Jumper:SolderJumper-2_P1.3mm_Open_RoundedPad1.0x1.5mm
- removed J_JTAG3V3_1, J_PROG3V3_1: Conn_01x02_Pin, Connector_PinHeader_2.54mm:PinHeader_1x02_P2.54mm_Vertical
- removed R1: 240, Resistor_SMD:R_0805_2012Metric
- removed R4: 60, Resistor_SMD:R_0805_2012Metric_Pad1.20x1.40mm_HandSolder
- removed R5: 390, Resistor_SMD:R_0805_2012Metric
- added 3V3LED2: LED, LED_SMD:LED_0805_2012Metric_Pad1.15x1.40mm_HandSolder, F.Cu at (62.3, 59.9)
- added C54: 1uF, Capacitor_SMD:C_0805_2012Metric_Pad1.18x1.45mm_HandSolder, F.Cu at (50.9, 79.6)
- added C55: 1uF, Capacitor_SMD:C_0805_2012Metric_Pad1.18x1.45mm_HandSolder, F.Cu at (40.5, 73.3)
- added J8: Conn_01x04_Pin, OverlordCommon:Solder_select_2x2, F.Cu at (174.6, 76.3)
- added J9: Conn_01x04_Pin, OverlordCommon:Solder_select_2x2, F.Cu at (163.0, 65.8)
- added R60: 240, Resistor_SMD:R_0805_2012Metric, F.Cu at (37.9, 79.6)
- added R61: 60, Resistor_SMD:R_0805_2012Metric_Pad1.20x1.40mm_HandSolder, F.Cu at (67.0, 59.8)
- added R62: 390, Resistor_SMD:R_0805_2012Metric, F.Cu at (34.2, 83.7)
- added U_LM317_3: LM317_SOT-223, Package_TO_SOT_SMD:SOT-223-3_TabPin2, F.Cu at (45.7, 78.2)
- D4: value 1N4148 -> SD0805S020S1R0
- moved C4 19.0 mm to (46.8, 65.3), turned to 90 degrees
- moved D4 12.8 mm to (50.6, 71.2)
- moved D5 9.26 mm to (33.0, 71.3), turned to 180 degrees
- moved U_LM317_1 8.94 mm to (41.5, 65.7)
- moved D2 7.51 mm to (46.0, 84.3), turned to 180 degrees
- moved C7 7.51 mm to (36.9, 74.5)
- moved R17 6.74 mm to (29.9, 80.5), turned to 0 degrees
- moved D1 5.38 mm to (46.8, 69.6), turned to -90 degrees
- moved C6 3.60 mm to (33.4, 77.3)
- moved R11 2.84 mm to (29.5, 74.4), turned to -90 degrees
- moved JP38 2.34 mm to (130.9, 71.2)
- moved DB9_OUT1 0.42 mm to (103.5, 101.7)
- moved DB9_IN1 0.18 mm to (155.9, 101.7)
- moved J1 0.10 mm to (33.0, 31.5)
- moved J2 0.10 mm to (85.7, 31.5)
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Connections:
- C4 pad 1: Net-(D1-K) -> USB+5V
- C6 pad 1: Net-(D5-K) -> +12V
- D1 pad 1: Net-(D1-K) -> USB+5V
- D2 pad 1: Net-(D1-K) -> +12V
- D2 pad 2: +12V -> +3.3V
- D5 pad 1: Net-(D5-K) -> +12V
- DB9_IN1 pad 1: GND -> MB2_H
- DB9_IN1 pad 2: CAN_L -> MB2_L
- DB9_IN1 pad 4: MB2_L -> CAN_L
- DB9_IN1 pad 5: MB2_H -> GND
- DB9_IN1 pad 6: MB1_L -> +12V
- DB9_IN1 pad 7: CAN_H -> MB1_H
- DB9_IN1 pad 8: MB1_H -> CAN_H
- DB9_IN1 pad 9: +12V -> MB1_L
- JP38 pad 1: Net-(JP38-A) -> +3.3V
- JP49 pad 2: Net-(JP49-B) -> +3.3V
- J_JTAG1 pad 10: Net-(JP47-A) -> unconnected-(J_JTAG1-Pad10)
- J_JTAG1 pad 2: Net-(JP39-A) -> JTAG_TMS
- J_JTAG1 pad 3: Net-(JP40-B) -> GND
- J_JTAG1 pad 4: Net-(JP41-A) -> JTAG_TCK
- J_JTAG1 pad 5: Net-(JP42-B) -> GND
- J_JTAG1 pad 6: Net-(JP43-A) -> JTAG_TDO
- J_JTAG1 pad 7: Net-(JP44-B) -> GND
- J_JTAG1 pad 8: Net-(JP45-A) -> JTAG_TDI
- J_JTAG1 pad 9: Net-(JP46-B) -> GND
- J_PROG1 pad 1: Net-(JP48-B) -> ESP_EN
- J_PROG1 pad 3: Net-(JP50-B) -> UART_TX_0
- J_PROG1 pad 4: Net-(JP51-A) -> GND
- J_PROG1 pad 5: Net-(JP52-B) -> UART_RX_0
- J_PROG1 pad 6: Net-(JP53-A) -> ESP_IO0
- U_LM317_1 pad 1: Net-(U_LM317_1-ADJ) -> V_ADJ
- U_LM317_1 pad 3: Net-(D1-K) -> USB+5V
- U_LM317_2 pad 3: Net-(D5-K) -> +12V
- U_TRS3232EIPWR1 pad 11: UART_TX_0 -> Net-(J9-Pin_1)
- U_TRS3232EIPWR1 pad 12: RS232_RX -> Net-(J9-Pin_2)
- U_TRS3232EIPWR1 pad 13: UART_RX_0 -> Net-(J8-Pin_1)
- U_TRS3232EIPWR1 pad 14: RS232_TX -> Net-(J8-Pin_2)
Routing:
- net V_ADJ: track 0.00 -> 47.5 mm
- net +3.3V: track 884.8 -> 917.8 mm, vias 2 -> 5
- net MB2_L: track 121.2 -> 150.2 mm
- net +12V: track 248.4 -> 276.3 mm, vias 1 -> 2
- net +5V: track 435.5 -> 409.7 mm, vias 1 -> 2
- net USB+5V: track 105.7 -> 84.8 mm, vias 2 -> 1
- net Net-(J9-Pin_1): track 0.00 -> 19.4 mm, vias 0 -> 2
- net Net-(D1-K): track 18.6 -> 0.00 mm
- net Net-(D5-K): track 18.5 -> 0.00 mm
- net MB1_L: track 134.1 -> 120.2 mm
- net S1: track 198.1 -> 210.9 mm
- net 1_1Y2: track 42.9 -> 30.4 mm
- net CAN_H: track 160.0 -> 171.9 mm
- net Net-(J8-Pin_1): track 0.00 -> 11.5 mm, vias 0 -> 2
- net 1_1Y0: track 43.6 -> 32.2 mm
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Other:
- board size 155.1 x 86.1 mm -> 155.7 x 86.3 mm
- board text added: "--- Overlord Actual --- Ver 2.0 Rev B"
- board text added: "74HC4052D"
- board text added: "BOOT"
- board text added: "CAN Termination"
- board text added: "CAN_L CAN_H CAN_RX CAN_TX"
- board text added: "Cable dir"
- board text added: "DB9 IN"
- board text added: "DB9 OUT"
- board text added: "ESP32-S3-WROOM-1U-N16"
- board text added: "ESP_EN"
- board text added: "ESP_IO0"
- board text added: "JTAG"
- board text added: "JTAG 3V3"
- board text added: "LM317"
- board text added: "MAX485ESA+T"
- board text added: "MX_RX_1 MB_DIR_1 MB_TX_1 MB1_H MB1_L"
- board text added: "MX_RX_2 MB_DIR_2 MB_TX_2 MB2_H MB2_L"
- board text added: "PROG"
- board text added: "PROG 3V3"
- board text added: "RESET"
- board text added: "SN65HVD230"
- board text added: "TRS3232EIPWR"
- board text added: "USB+5V +3.3V +5V +12V"
- board text removed: "--- Overlord Actual --- Ver 2.0 Rev A"
